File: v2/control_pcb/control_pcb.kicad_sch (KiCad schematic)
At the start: 16 parts, among them J1 Raspberry_Pi_2_3, J10 8P8C_Shielded, J2 8P8C_Shielded, J6 Screw_Terminal_01x02, J7 Screw_Terminal_01x02, J8 Screw_Terminal_01x08, J9 Screw_Terminal_01x08, U3 Raspberry_Pi_Pico_2

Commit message: Doing stuff
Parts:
- added C3, C4, C5: 0.1uF, Capacitor_THT:C_Rect_L4.6mm_W2.0mm_P2.50mm_MKS02_FKP02, symbol Device:C
- added J11, J12, J13: Screw_Terminal_01x02, TerminalBlock_Phoenix:TerminalBlock_Phoenix_PT-1,5-2-5.0-H_1x02_P5.00mm_Horizontal, symbol Connector:Screw_Terminal_01x02
- added U4: TCA9509DGKR, Package_SO:VSSOP-8_3x3mm_P0.65mm, symbol Logic_LevelTranslator:TCA9517ADGK
- added U5: TXB0104D, Package_SO:SOIC-14_3.9x8.7mm_P1.27mm, symbol Logic_LevelTranslator:TXB0104D
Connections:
- net +24V: now also J11.1 (Pin_1)
- net +3.3V: now also C5.1, U4.1 (VCCA), U5.1 (VCCA), U5.8 (OE)
- net +5V: now also U3.39 (VSYS), C3.1, C4.1, J13.1 (Pin_1), U4.5 (EN), U4.8 (VCCB), U5.14 (VCCB)
- net ALARM1+: now also U3.12 (GPIO9)
- net ALARM2+: now also U3.17 (GPIO13)
- net DIR1+: now also U3.10 (GPIO7)
- net DIR2+: now also U3.15 (GPIO11)
- net ENA1+: now also U3.11 (GPIO8)
- net ENA2+: now also U3.16 (GPIO12)
- net GND: now also J1.14 (GND), J1.20 (GND), J1.25 (GND), J1.30 (GND), J1.34 (GND), J1.39 (GND), J1.6 (GND), J1.9 (GND), U3.13 (GND), U3.18 (GND), U3.23 (GND), U3.28 (GND), U3.3 (GND), U3.33 (GND), U3.38 (GND), U3.8 (GND), C3.2, C4.2, C5.2, J11.2 (Pin_2), J12.2 (Pin_2), J13.2 (Pin_2), U4.4 (GND), U5.7 (GND)
- net LIMIT_SW_LL: now also U3.4 (GPIO2)
- net LIMIT_SW_LR: now also U3.5 (GPIO3)
- net LIMIT_SW_RL: now also U3.6 (GPIO4)
- net LIMIT_SW_RR: now also U3.7 (GPIO5)
- net PUL1+: now also U3.9 (GPIO6)
- net PUL2+: now also U3.14 (GPIO10)
- net SPI_MOSI: now reaches U3.21 (GPIO16)
- net SPI_MOSI: now also U5.11 (B3)
- net SPI_CS: now reaches U3.22 (GPIO17)
- net SPI_CS: now also U5.13 (B1)
- net SPI_SCLK: now reaches U3.24 (GPIO18)
- net SPI_SCLK: now also U5.10 (B4)
- net SPI_MISO: now reaches U3.25 (GPIO19)
- net SPI_MISO: now also U5.12 (B2)
- net SPI_MOSI_3.3: now reaches J1.19 (MOSI0/GPIO10)
- net SPI_MOSI_3.3: now also U5.4 (A3)
- net SPI_MISO_3.3: now reaches J1.21 (MISO0/GPIO9)
- net SPI_MISO_3.3: now also U5.3 (A2)
- net SPI_SCLK_3.3: now reaches J1.23 (SCLK0/GPIO11)
- net SPI_SCLK_3.3: now also U5.5 (A4)
- net SPI_CS_3.3: now reaches J1.24 (~{CE0}/GPIO8)
- net SPI_CS_3.3: now also U5.2 (A1)
- net SDA_3.3: now reaches J1.3 (SDA/GPIO2)
- net SDA_3.3: now also U4.3 (SDAA)
- net SCL_3.3: now reaches J1.5 (SCL/GPIO3)
- net SCL_3.3: now also U4.2 (SCLA)
- new net +12V: J12.1 (Pin_1)
- new net SCL: U4.7 (SCLB)
- new net SDA: U4.6 (SDAB)
- no-connect marks 0 -> 37
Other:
- added sheet Current Sensing (current_sensing.kicad_sch)
- moved on the sheet: D1, D2, H1, H2, H3, H4, J10, J2, J6, J7, J8, J9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

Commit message: Added TXU0304 level shifter
Added unidirectional SPI compatible level shifter
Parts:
- removed U5: TXB0104D, Package_SO:SOIC-14_3.9x8.7mm_P1.27mm, symbol Logic_LevelTranslator:TXB0104D
- added U5: TXU0304PWR, Package_SO:TSSOP-14_4.4x5mm_P0.65mm, symbol bh_symbol_library:TXU0304PWR
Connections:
- net +3.3V: now also U5.1 (VCCA), U5.8 (OE)
- net +5V: now also U5.14 (VCCB)
- net GND: now also U5.7 (GND)
- net SPI_CS: now also U5.13 (B1)
- net SPI_CS_3.3: now also U5.2 (A1)
- net SPI_MISO: now also U5.10 (B4)
- net SPI_MISO_3.3: now also U5.5 (A4)
- net SPI_MOSI: now also U5.11 (B3)
- net SPI_MOSI_3.3: now also U5.4 (A3)
- net SPI_SCLK: now also U5.12 (B2)
- net SPI_SCLK_3.3: now also U5.3 (A2)
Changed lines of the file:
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@@
 	(global_label "SPI_MISO"
 		(shape input)
-		(at 83.82 121.92 0)
+		(at 83.82 132.08 0)
 		(fields_autoplaced yes)
 		(effects
@@
 		)
 		(property "Intersheetrefs" "${INTERSHEET_REFS}"
-			(at 95.4533 121.92 0)
+			(at 95.4533 132.08 0)
 			(effects
 				(font
@@
 	(global_label "SPI_SCLK"
 		(shape input)
-		(at 83.82 132.08 0)
+		(at 83.82 121.92 0)
 		(fields_autoplaced yes)
 		(effects
@@
 		)
 		(property "Intersheetrefs" "${INTERSHEET_REFS}"
-			(at 95.6347 132.08 0)
+			(at 95.6347 121.92 0)
 			(effects
 				(font
@@
 	(global_label "SPI_MISO_3.3"
 		(shape input)
-		(at 63.5 121.92 180)
+		(at 63.5 132.08 180)
 		(fields_autoplaced yes)
 		(effects
@@
 		)
 		(property "Intersheetrefs" "${INTERSHEET_REFS}"
-			(at 47.8753 121.92 0)
+			(at 47.8753 132.08 0)
 			(effects
 				(font
@@
 	(global_label "SPI_SCLK_3.3"
 		(shape input)
-		(at 63.5 132.08 180)
+		(at 63.5 121.92 180)
 		(fields_autoplaced yes)
 		(effects
@@
 		)
 		(property "Intersheetrefs" "${INTERSHEET_REFS}"
-			(at 47.6939 132.08 0)
+			(at 47.6939 121.92 0)
 			(effects
 				(font
@@
 	)
 	(symbol
+		(lib_id "bh_symbol_library:TXU0304PWR")
+		(at 66.04 109.22 0)
+		(unit 1)
+		(exclude_from_sim no)
+		(in_bom yes)
+		(on_board yes)
+		(dnp no)
+		(fields_autoplaced yes)
+		(property "Reference" "U5"
+			(at 75.8541 142.24 0)
+			(effects
+				(font
+					(size 1.27 1.27)
+				)
+				(justify left)
+			)
+		)
+		(property "Value" "TXU0304PWR"
+			(at 75.8541 144.78 0)
+			(show_name yes)
+			(effects
+				(font
+					(size 1.27 1.27)
+				)
+				(justify left)
+			)
+		)
+		(property "Footprint" "Package_SO:TSSOP-14_4.4x5mm_P0.65mm"
+			(at 66.04 111.76 0)
+			(effects
+				(font
+					(size 1.27 1.27)
+				)
+				(hide yes)
+			)
+		)
+		(property "Datasheet" ""
+			(at 66.04 111.76 0)
+			(effects
+				(font
+					(size 1.27 1.27)
+				)
+				(hide yes)
+			)
+		)
+		(property "Description" ""
+			(at 66.04 111.76 0)
+			(effects
+				(font
+					(size 1.27 1.27)
+				)
+				(hide yes)
+			)
+		)
+		(pin "8"
+		)
+		(pin "5"
+		)
+		(pin "11"
+		)
+		(pin "2"
+		)
+		(pin "6"
+		)
+		(pin "12"
+		)
+		(pin "9"
+		)
+		(pin "10"
+		)
+		(pin "4"
+		)
+		(pin "3"
+		)
+		(pin "14"
+		)
+		(pin "7"
+		)
+		(pin "1"
+		)
+		(pin "13"
+		)
+		(instances
+			(project ""
+				(path "/bfe9039d-f086-4b10-bdde-e613b3218973"
+					(reference "U5")
+					(unit 1)
+				)
+			)
+		)
+	)
+	(symbol
 		(lib_id "power:+5V")
 		(at 50.8 26.67 0)
@@
 					(unit 1)
 				)
-			)
-		)
-	)
-	(symbol
-		(lib_id "Logic_LevelTranslator:TXB0104D")
-		(at 73.66 124.46 0)
-		(unit 1)
-		(exclude_from_sim no)
-		(in_bom yes)
-		(on_board yes)
-		(dnp no)
-		(fields_autoplaced yes)
-		(property "Reference" "U5"
-			(at 75.8541 142.24 0)
-			(effects
-				(font
-					(size 1.27 1.27)
-				)
-				(justify left)
-			)
-		)
-		(property "Value" "TXB0104D"
-			(at 75.8541 144.78 0)
-			(effects
-				(font
-					(size 1.27 1.27)
-				)
-				(justify left)
-			)
-		)
-		(property "Footprint" "Package_SO:SOIC-14_3.9x8.7mm_P1.27mm"
-			(at 73.66 143.51 0)
-			(effects
-				(font
-					(size 1.27 1.27)
-				)
-				(hide yes)
-			)
-		)
-		(property "Datasheet" "http://www.ti.com/lit/ds/symlink/txb0104.pdf"
-			(at 76.454 122.047 0)
-			(effects
-				(font
-					(size 1.27 1.27)
-				)
-				(hide yes)
-			)
-		)
-		(property "Description" "4-Bit Bidirectional Voltage-Level Translator, Auto Direction Sensing and ±15-kV ESD Protection, 1.2 - 3.6V APort, 1.65 - 5.5V BPort, SOIC-14"
-			(at 73.66 124.46 0)
-			(effects
-				(font
-					(size 1.27 1.27)
-				)
-				(hide yes)
-			)
-		)
-		(pin "10"
-		)
-		(pin "1"
-		)
-		(pin "5"
-		)
-		(pin "13"
-		)
-		(pin "14"
-		)
-		(pin "4"
-		)
-		(pin "11"
-		)
-		(pin "12"
-		)
-		(pin "6"
-		)
-		(pin "3"
-		)
-		(pin "7"
-		)
-		(pin "2"
-		)
-		(pin "9"
-		)
-		(pin "8"
-		)
-		(instances
-			(project ""
-				(path "/bfe9039d-f086-4b10-bdde-e613b3218973"
-					(reference "U5")
-					(unit 1)
-				)

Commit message: Preliminary V2 schematics
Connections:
- net LED1: now also U3.1 (GPIO0)
- net LED2: now also U3.2 (GPIO1)
- no-connect marks 37 -> 35
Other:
- moved on the sheet: C3, C4, C5, D1, D2, H1, H2, H3, H4, J1, J10, J11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

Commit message: Doing stuff
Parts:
- added R17: 904R, Resistor_THT:R_Axial_DIN0207_L6.3mm_D2.5mm_P10.16mm_Horizontal, symbol Device:R_US
- added U8: LM404C30ILPR, Package_TO_SOT_THT:TO-92_Inline, symbol Reference_Voltage:LM4040LP-4.1
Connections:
- net +5V: now also R17.1
- net GND: now also U8.3 (A)
- net at U3.35 (VREF): now also R17.2, U8.2 (K)
- no-connect marks 35 -> 34
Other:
- moved on the sheet: U3

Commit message: Doing some things
Crossing some ts and dotting some is. Making v3 of the BOM.
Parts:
- U3: Digikey (none) -> https://www.digikey.ca/en/products/detail/raspberry-pi/SC16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
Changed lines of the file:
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@@
 		(on_board yes)
 		(dnp no)
-		(fields_autoplaced yes)
 		(property "Reference" "#PWR038"
 			(at 81.28 165.1 0)
@@
 		)
 		(property "Description" ""
+			(at 144.78 57.15 0)
+			(effects
+				(font
+					(size 1.27 1.27)
+				)
+				(hide yes)
+			)
+		)
+		(property "Digikey" "https://www.digikey.ca/en/products/detail/raspberry-pi/SC1631/24627136"
 			(at 144.78 57.15 0)
 			(effects
@@
 		(on_board yes)
 		(dnp no)
-		(fields_autoplaced yes)
 		(property "Reference" "#PWR039"
 			(at 86.36 165.1 0)

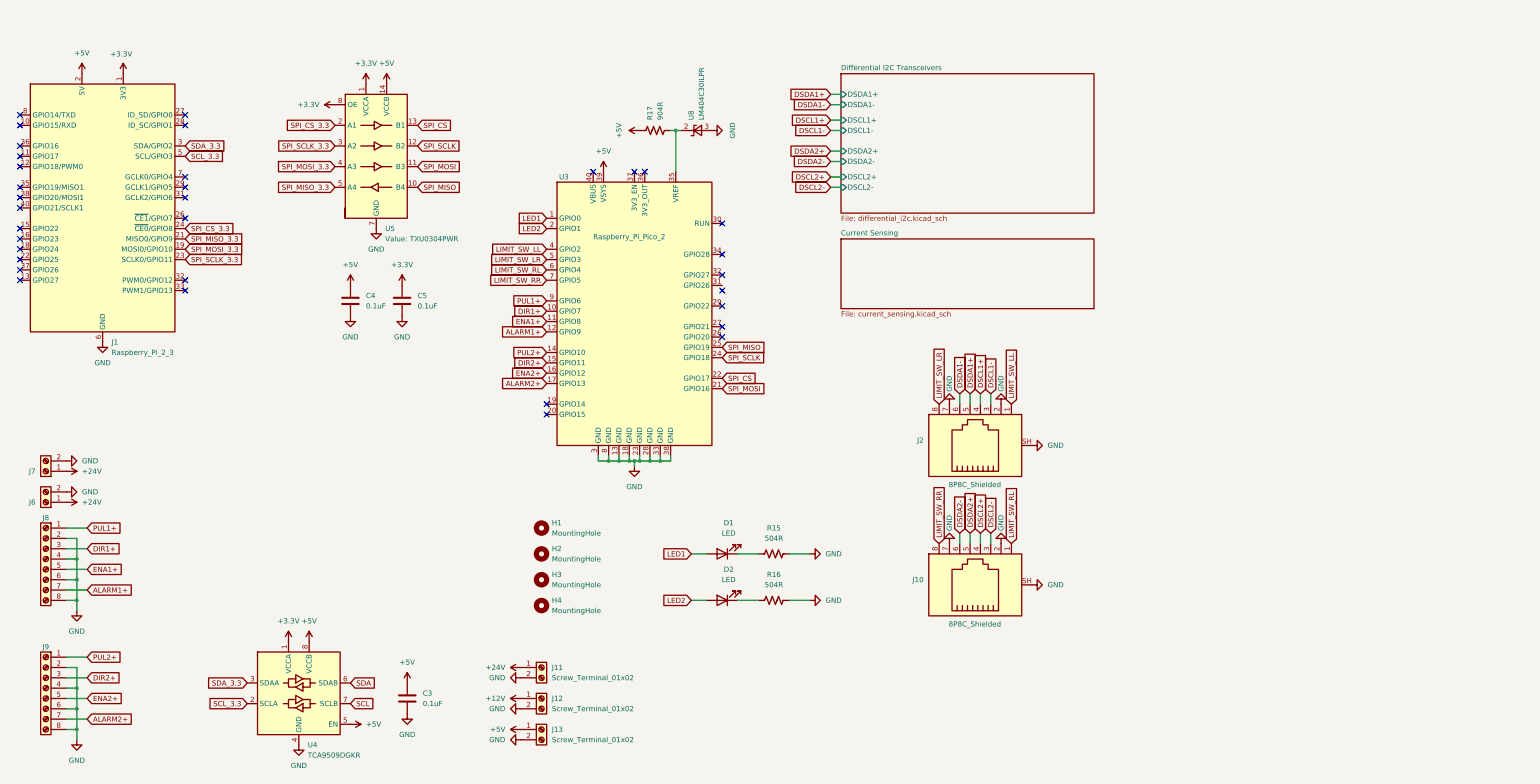
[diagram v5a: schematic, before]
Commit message: Switched logic level shifting from SPI to GPIO
RPi Pico uses 5V power in but has an internal 3.3V regulator so uses 3.3V logic. Level shifting not required for SPI then but required for GPIO pins going to stepper control outputs
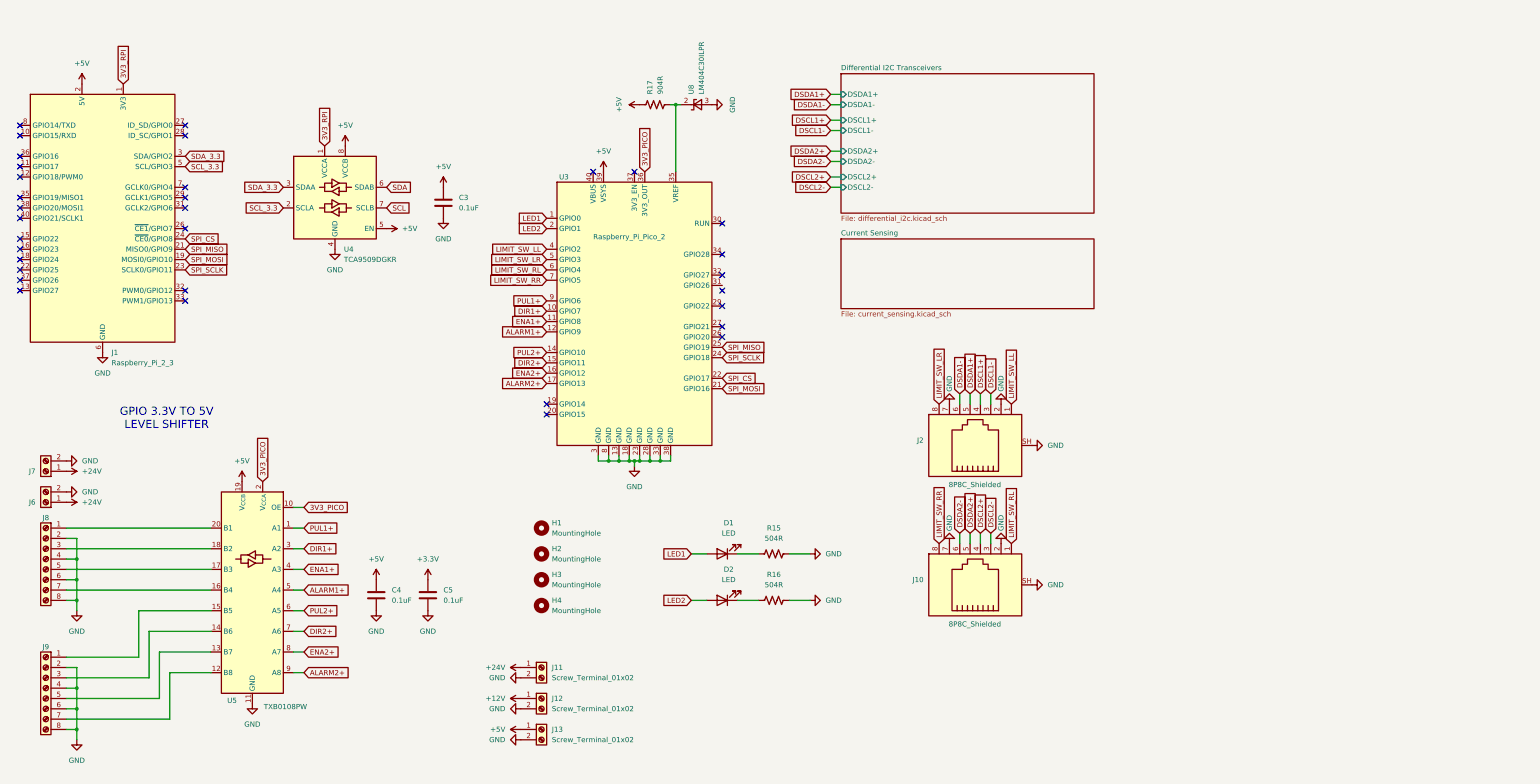
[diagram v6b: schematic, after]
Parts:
- removed U5: TXU0304PWR, Package_SO:TSSOP-14_4.4x5mm_P0.65mm, symbol bh_symbol_library:TXU0304PWR
- added U5: TXB0108PW, Package_SO:TSSOP-20_4.4x6.5mm_P0.65mm, symbol Logic_LevelTranslator:TXB0108PW
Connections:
- net SPI_CS_3.3 is gone; now on net SPI_CS: J1.24 (~{CE0}/GPIO8)
- net SPI_MISO_3.3 is gone; now on net SPI_MISO: J1.21 (MISO0/GPIO9)
- net SPI_MOSI_3.3 is gone; now on net SPI_MOSI: J1.19 (MOSI0/GPIO10)
- net SPI_SCLK_3.3 is gone; now on net SPI_SCLK: J1.23 (SCLK0/GPIO11)
- net +3.3V: no longer J1.1 (3V3), J1.17 (3V3), U4.1 (VCCA)
- net +5V: now also U5.19 (V_{CCB})
- net ALARM1+: now also U5.5 (A4); no longer J8.7 (Pin_7)
- net ALARM2+: now also U5.9 (A8); no longer J9.7 (Pin_7)
- net DIR1+: now also U5.3 (A2); no longer J8.3 (Pin_3)
- net DIR2+: now also U5.7 (A6); no longer J9.3 (Pin_3)
- net ENA1+: now also U5.4 (A3); no longer J8.5 (Pin_5)
- net ENA2+: now also U5.8 (A7); no longer J9.5 (Pin_5)
- net GND: now also U5.11 (GND)
- net PUL1+: now also U5.1 (A1); no longer J8.1 (Pin_1)
- net PUL2+: now also U5.6 (A5); no longer J9.1 (Pin_1)
- net 3V3_PICO: now reaches U3.36 (3V3_OUT)
- net 3V3_PICO: now also U5.10 (OE), U5.2 (V_{CCA})
- new net: J9.1 (Pin_1), U5.15 (B5)
- new net: J9.3 (Pin_3), U5.14 (B6)
- new net: J9.5 (Pin_5), U5.13 (B7)
- new net: J9.7 (Pin_7), U5.12 (B8)
- new net: J8.7 (Pin_7), U5.16 (B4)
- new net: J8.5 (Pin_5), U5.17 (B3)
- new net: J8.3 (Pin_3), U5.18 (B2)
- new net: J8.1 (Pin_1), U5.20 (B1)
- new net 3V3_RPI: J1.1 (3V3), J1.17 (3V3), U4.1 (VCCA)
- no-connect marks 34 -> 33
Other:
- note added: "GPIO 3.3V TO 5V LEVEL SHIFTER"
- moved on the sheet: C3, J1, R17, U4, U8

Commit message: Doing some things
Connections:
- net ALARM1+: now also U3.17 (GPIO13), U5.1 (A1); no longer U3.12 (GPIO9), U5.5 (A4)
- net ALARM2+: now also U3.12 (GPIO9), U5.6 (A5); no longer U3.17 (GPIO13), U5.9 (A8)
- net DIR1+: now also U3.15 (GPIO11), U5.4 (A3); no longer U3.10 (GPIO7), U5.3 (A2)
- net DIR2+: now also U3.10 (GPIO7), U5.8 (A7); no longer U3.15 (GPIO11), U5.7 (A6)
- net ENA1+: now also U3.16 (GPIO12), U5.3 (A2); no longer U3.11 (GPIO8), U5.4 (A3)
- net ENA2+: now also U3.11 (GPIO8), U5.7 (A6); no longer U3.16 (GPIO12), U5.8 (A7)
- net PUL1+: now also U3.14 (GPIO10), U5.5 (A4); no longer U3.9 (GPIO6), U5.1 (A1)
- net PUL2+: now also U3.9 (GPIO6), U5.9 (A8); no longer U3.14 (GPIO10), U5.6 (A5)

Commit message: Doing more things
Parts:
- removed R17: 904R, Resistor_THT:R_Axial_DIN0207_L6.3mm_D2.5mm_P10.16mm_Horizontal, symbol Device:R_US
- removed U8: LM404C30ILPR, Package_TO_SOT_THT:TO-92_Inline, symbol Reference_Voltage:LM4040LP-4.1
- added C7: 0.1uF, Capacitor_THT:C_Rect_L4.6mm_W2.0mm_P2.50mm_MKS02_FKP02, symbol Device:C
- added R24, R25: 10kR, Resistor_THT:R_Axial_DIN0207_L6.3mm_D2.5mm_P10.16mm_Horizontal, symbol Device:R_US
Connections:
- net +3.3V is gone; now on net 3V3_PICO: C5.1
- net 3V3_RPI: now also C7.1, R24.1, R25.1
- net GND: now also C7.2
- net SCL_3.3: now also R25.2
- net SDA_3.3: now also R24.2
- no-connect marks 33 -> 34
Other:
- moved on the sheet: C3
